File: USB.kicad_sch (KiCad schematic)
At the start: 8 parts, among them J23 USB_B_Micro, U19 CP2102N-A01-GQFN24

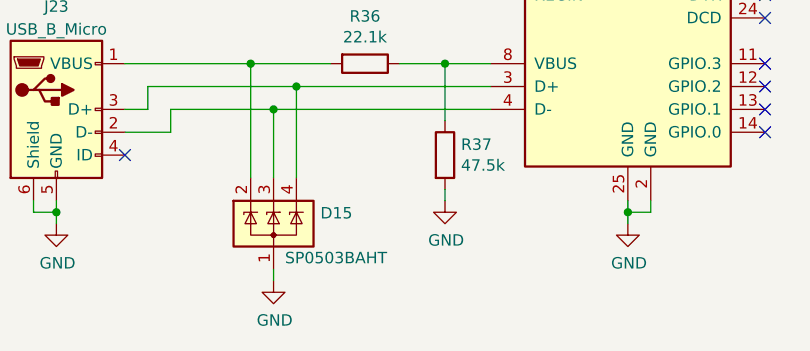
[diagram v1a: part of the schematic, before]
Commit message: Schematic notations for rework changes
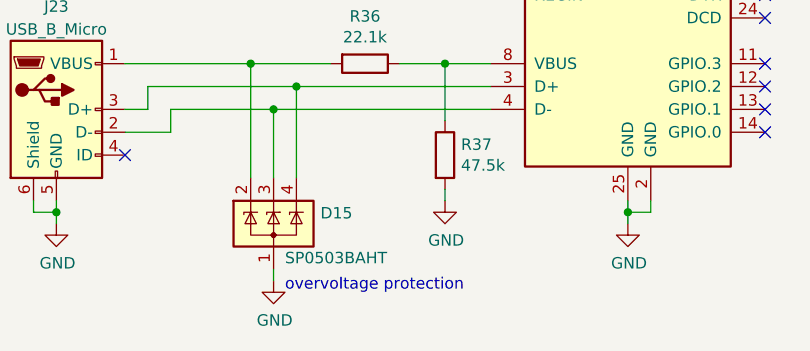
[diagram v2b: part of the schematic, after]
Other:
- note added: "overvoltage protection"

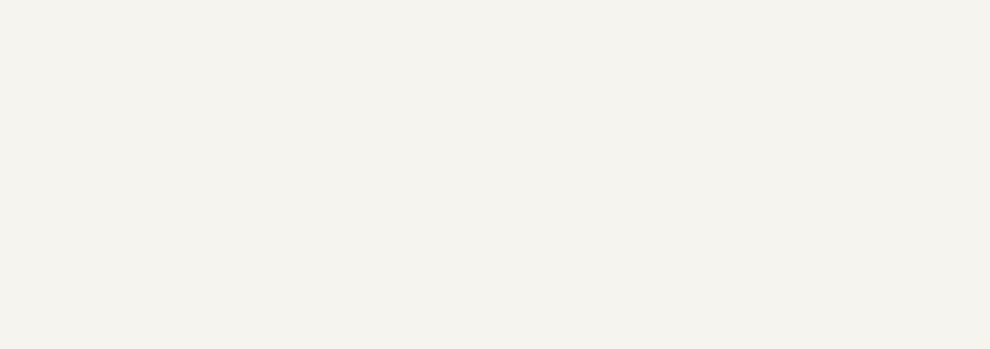
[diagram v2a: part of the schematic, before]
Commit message: Updated schematic in accordance to previous weeks annotated changes
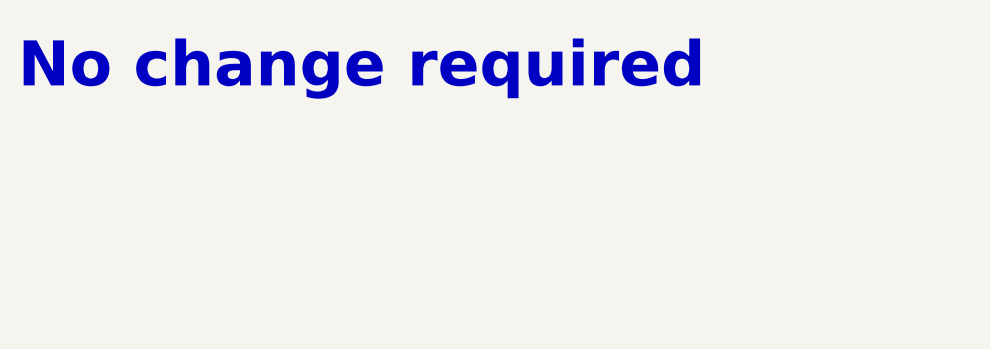
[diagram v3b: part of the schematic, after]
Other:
- note added: "No change required"
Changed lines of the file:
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@@
     (effects (font (size 1.27 1.27) (color 255 4 0 1)) (justify left bottom))
+  )
+  (text "No change required\n" (at 15.24 21.59 0)
+    (effects (font (face "KiCad Font") (size 5 5) (thickness 1) bold (color 255 2 13 1)) (justify left bottom))
   )
   (hierarchical_label "UART_RX" (shape input) (at 166.37 88.9 0) (fields_autoplaced)

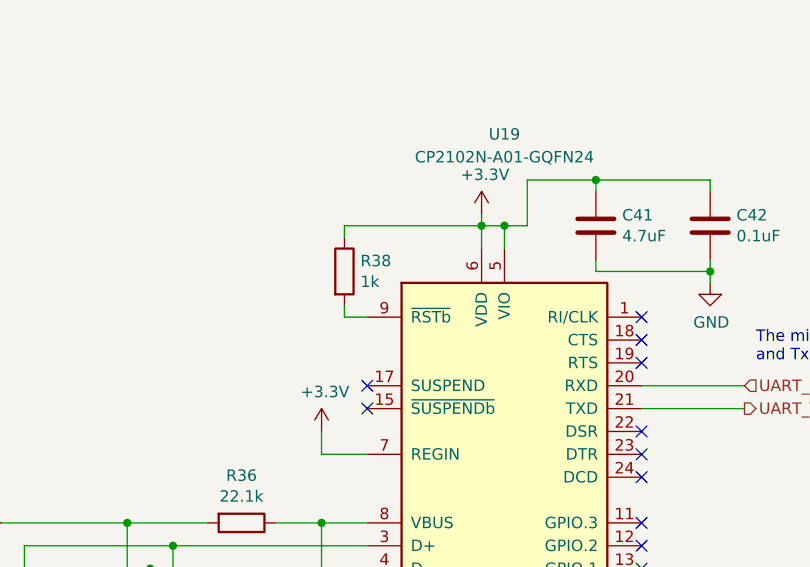
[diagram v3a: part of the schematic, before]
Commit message: Renamed Clk to PA5, removed CAN_TX/RX test points, deleted other .lck file and #auto_saved_files# (hopefully this does not break anything.
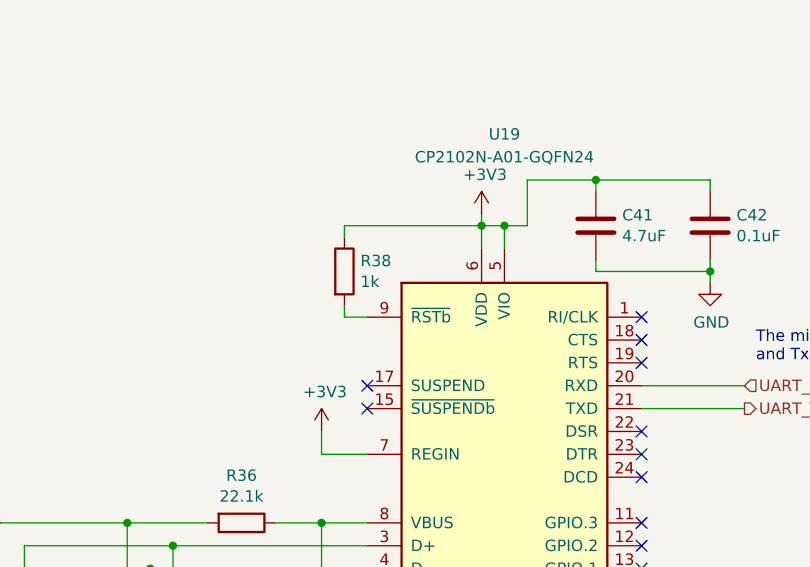
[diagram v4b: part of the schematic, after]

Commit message: fixed some footprints and part numbers
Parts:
- C41: Mouser Part Number 80-C0805C475K3RAUTO -> 81-GRM219R6YA475KA3D
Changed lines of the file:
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@@
 			)
 		)
-		(property "Mouser Part Number" "80-C0805C475K3RAUTO "
+		(property "Mouser Part Number" "81-GRM219R6YA475KA3D"
 			(at 149.86 71.12 0)
 			(effects

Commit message: Added/checked datasheet links/part numbers, deleted accel_pot2 and brake_pot2 hierarchical labels and changed corresponding pins (PC2, PC3) to GPIO on the now-2x5 extra GPIO connector.
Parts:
- C42: Mouser Part Number 80-C0805C104K3R -> 80-C0805C104M5R
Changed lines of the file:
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@@
 			)
 		)
-		(property "Datasheet" "~"
+		(property "Datasheet" "https://www.mouser.com/ProductDetail/71-CRCW0805-47.5K-E3"
 			(at 119.38 114.3 0)
 			(effects
@@
 			)
 		)
-		(property "Datasheet" "~"
+		(property "Datasheet" "https://www.mouser.com/ProductDetail/Vishay-Dale/CRCW080522K1FKEA?qs=fIsz7OpyEY%2F1GKOToH8JbQ%3D%3D"
 			(at 110.49 104.14 0)
 			(effects
@@
 			)
 		)
-		(property "Datasheet" "~"
+		(property "Datasheet" "https://www.mouser.com/ProductDetail/Vishay-Dale/CRCW08051K00FKEAC?qs=CZ6xfwOSLTXmQIgaYvN%2FBA%3D%3D"
 			(at 121.92 76.2 0)
 			(effects
@@
 			)
 		)
-		(property "Datasheet" "~"
+		(property "Datasheet" "https://www.mouser.com/ProductDetail/Murata-Electronics/GRM219R6YA475KA73D?qs=eeBpzGFlv%252B%252Bho6epIC%2FPCA%3D%3D&srsltid=AfmBOor8KpuDmhbErgZyZAx51mjKq7YIEoZ5aJP4Jbdc10duuv9ImkWI"
 			(at 149.86 71.12 0)
 			(effects
@@
 			)
 		)
-		(property "Datasheet" "~"
+		(property "Datasheet" "https://www.mouser.com/ProductDetail/KEMET/C0805C104M5RACTU?qs=VOOUd%252Bza08qHu13WgNByHQ%3D%3D"
 			(at 162.56 71.12 0)
 			(effects
@@
 			)
 		)
-		(property "Mouser Part Number" "80-C0805C104K3R "
+		(property "Mouser Part Number" "80-C0805C104M5R"
 			(at 162.56 71.12 0)
 			(effects
